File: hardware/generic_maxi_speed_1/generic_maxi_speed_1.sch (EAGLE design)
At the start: 30 parts, among them IC1 MEGA168/328, IC2 RFM12, IC3 LP2950Z, Q1 20MHz

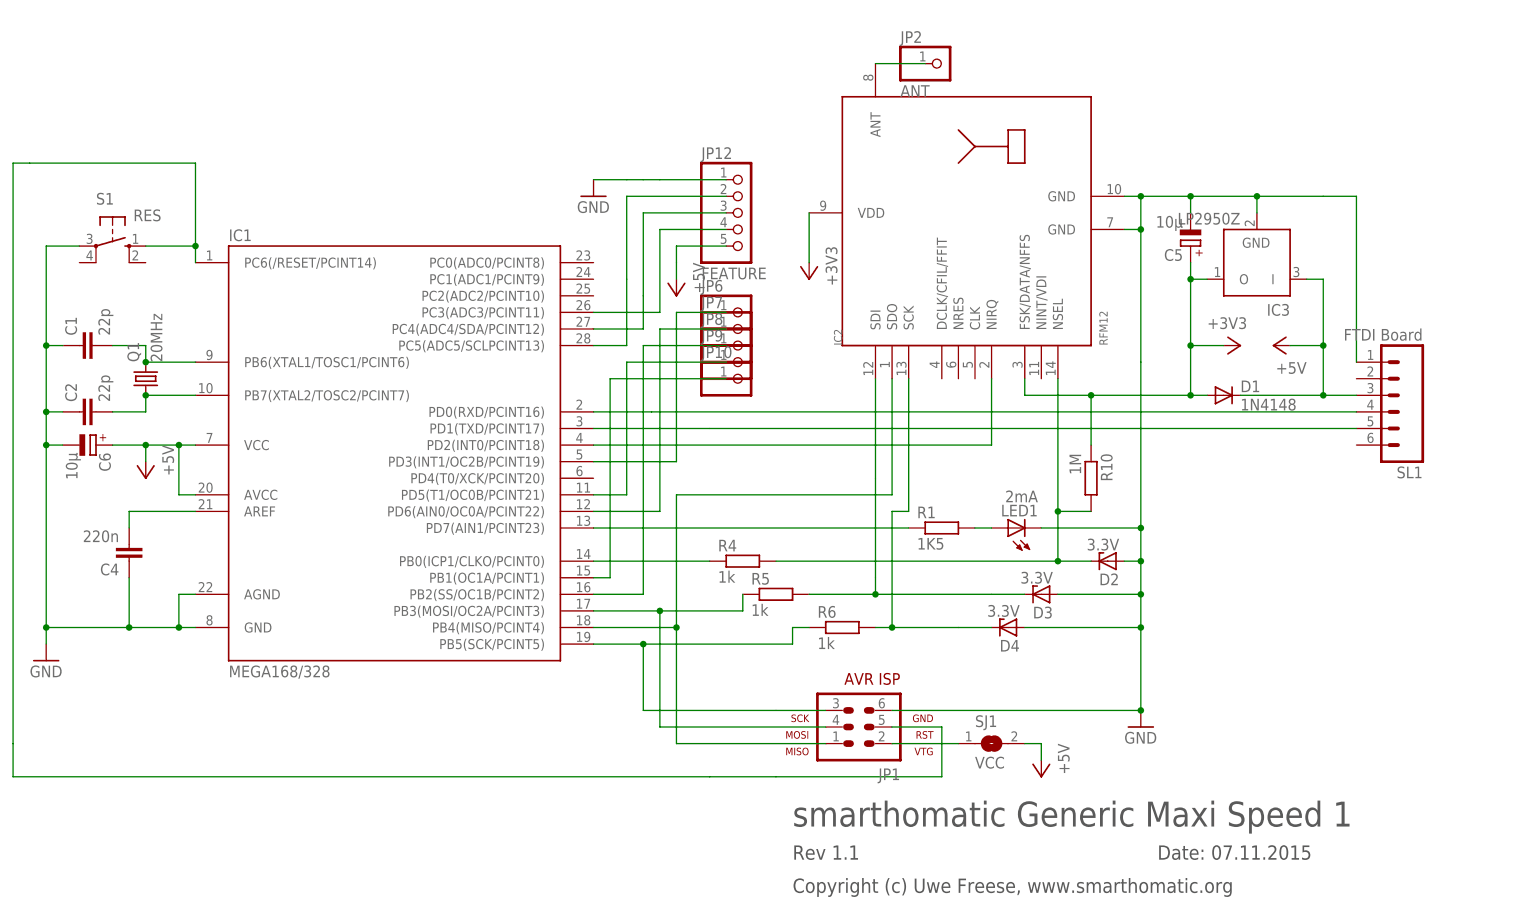
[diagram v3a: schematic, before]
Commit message: Generic Maxi Speed V1.2: Added transistor to switch power of RFM module to allow restart or module if transceiver doesn't react anymore.
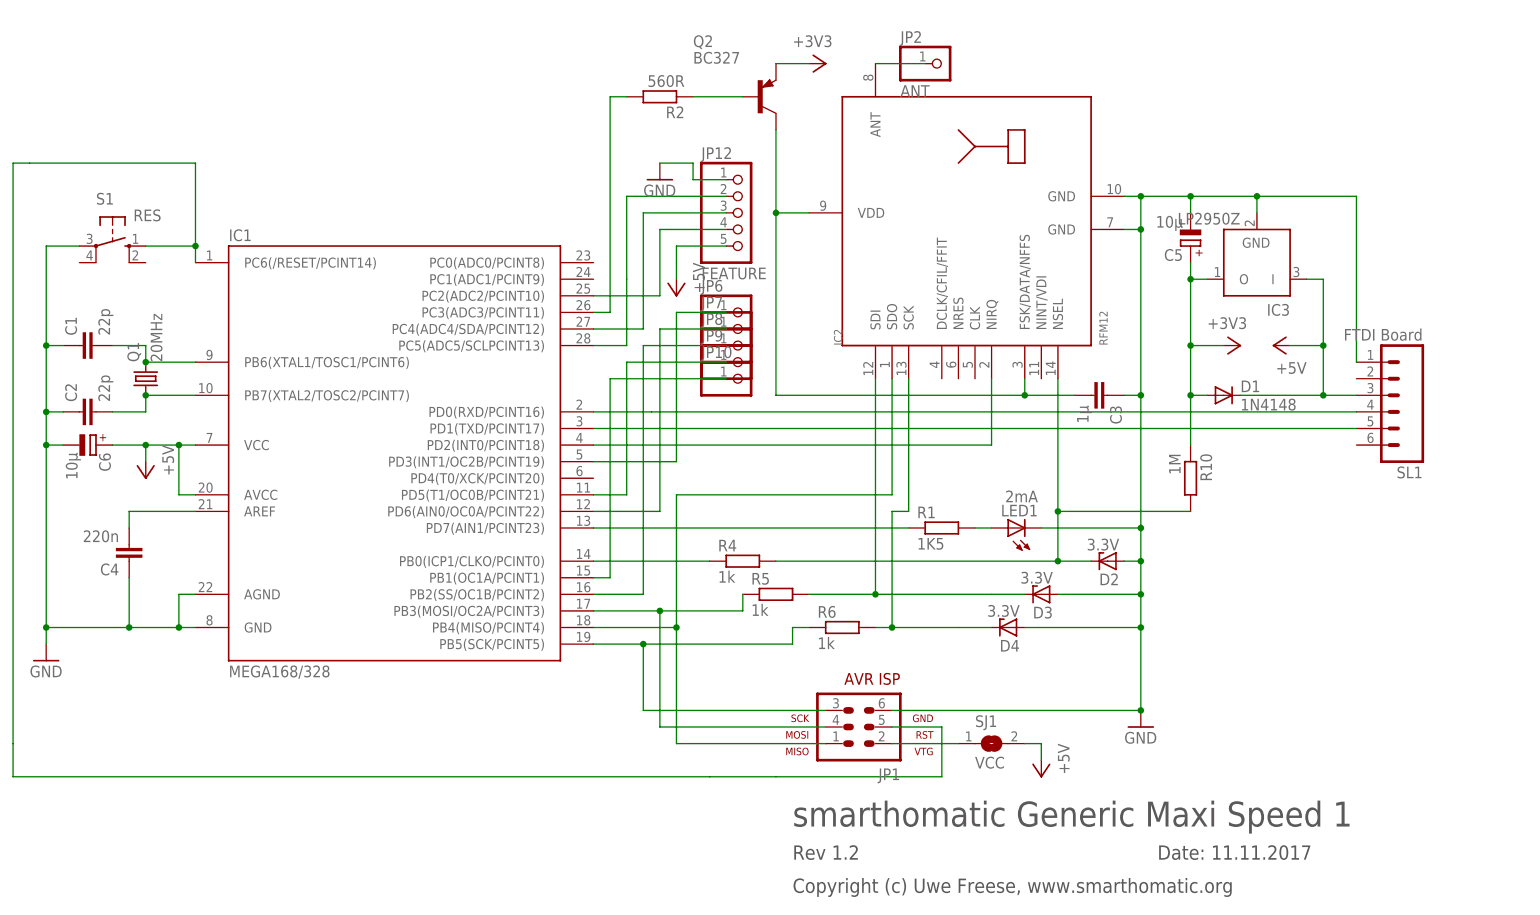
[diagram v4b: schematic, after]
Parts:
- added C3: 1µ, rcl:C-EU025-030X050
- added Q2: BC327, transistor-pnp:BC327
- added R2: 560R, rcl:R-EU_0207/7
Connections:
- new net N$28: IC1.PC3(ADC3/PCINT11), R2.2
- new net N$29: Q2.B, R2.1
- new net N$32: C3.2, IC2.FSK/DATA/NFFS, IC2.VDD, Q2.C
- net +3V3: now also Q2.E; no longer IC2.FSK/DATA/NFFS, IC2.VDD
- net GND: now also C3.1
- net N$14: now also IC1.PC2(ADC2/PCINT10); no longer IC1.PC3(ADC3/PCINT11)
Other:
- note added: "Date: 11.11.2017"
- note added: "Rev 1.2"
- note removed: "Date: 07.11.2015"
- note removed: "Rev 1.1"
- moved on the sheet: R10
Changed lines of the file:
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@@
 <?xml version="1.0" encoding="utf-8"?>
 <!DOCTYPE eagle SYSTEM "eagle.dtd">
-<eagle version="7.3.0">
+<eagle version="7.1.0">
 <drawing>
 <settings>
@@
 <part name="SJ1" library="jumper" deviceset="SJ" device="" value="VCC"/>
 <part name="P+3" library="supply1" deviceset="+5V" device=""/>
+<part name="Q2" library="transistor-pnp" deviceset="BC327" device=""/>
+<part name="R2" library="rcl" deviceset="R-EU_" device="0207/7" value="560R"/>
+<part name="C3" library="rcl" deviceset="C-EU" device="025-030X050" value="1µ"/>
 </parts>
 <sheets>
@@
 <frame x1="-60.96" y1="-58.42" x2="172.72" y2="93.98" columns="8" rows="5" layer="97"/>
 <text x="66.04" y="-40.64" size="3.81" layer="97">smarthomatic Generic Maxi Speed 1</text>
-<text x="121.92" y="-45.72" size="2.1844" layer="97">Date: 07.11.2015</text>
-<text x="66.04" y="-45.72" size="2.1844" layer="97">Rev 1.1</text>
+<text x="121.92" y="-45.72" size="2.1844" layer="97">Date: 11.11.2017</text>
+<text x="66.04" y="-45.72" size="2.1844" layer="97">Rev 1.2</text>
 <text x="66.04" y="-50.8" size="2.1844" layer="97">Copyright (c) Uwe Freese, www.smarthomatic.org</text>
 </plain>
@@
 <attribute name="NAME" x="162.56" y="14.478" size="1.778" layer="95" rot="R180"/>
 </instance>
-<instance part="GND3" gate="1" x="35.56" y="55.88"/>
-<instance part="R10" gate="G$1" x="111.76" y="12.7" rot="R270"/>
+<instance part="GND3" gate="1" x="45.72" y="58.42"/>
+<instance part="R10" gate="G$1" x="127" y="12.7" rot="R270"/>
 <instance part="C1" gate="G$1" x="-43.18" y="33.02" rot="R90"/>
 <instance part="C2" gate="G$1" x="-43.18" y="22.86" rot="R90"/>
@@
 <instance part="IC3" gate="G$1" x="137.16" y="45.72" rot="R180"/>
 <instance part="D1" gate="G$1" x="132.08" y="25.4"/>
-<instance part="+3V1" gate="G$1" x="68.58" y="43.18" rot="R180"/>
+<instance part="+3V1" gate="G$1" x="71.12" y="76.2" rot="R270"/>
 <instance part="P+4" gate="1" x="-33.02" y="12.7" rot="R180"/>
 <instance part="P+1" gate="1" x="139.7" y="33.02" rot="R90"/>
@@
 <instance part="SJ1" gate="1" x="96.52" y="-27.94"/>
 <instance part="P+3" gate="1" x="104.14" y="-33.02" rot="R180"/>
+<instance part="Q2" gate="G$1" x="60.96" y="71.12"/>
+<instance part="R2" gate="G$1" x="45.72" y="71.12" rot="R180"/>
+<instance part="C3" gate="G$1" x="114.3" y="25.4" rot="R270"/>
 </instances>
 <busses>
@@
 <wire x1="81.28" y1="-22.86" x2="119.38" y2="-22.86" width="0.1524" layer="91"/>
 <pinref part="GND2" gate="1" pin="GND"/>
-<wire x1="119.38" y1="30.48" x2="119.38" y2="5.08" width="0.1524" layer="91"/>
 <junction x="119.38" y="-22.86"/>
 <pinref part="LED1" gate="G$1" pin="C"/>
+<wire x1="119.38" y1="25.4" x2="119.38" y2="5.08" width="0.1524" layer="91"/>
 <wire x1="119.38" y1="5.08" x2="119.38" y2="0" width="0.1524" layer="91"/>
 <wire x1="119.38" y1="0" x2="119.38" y2="-5.08" width="0.1524" layer="91"/>
@@
 <wire x1="104.14" y1="5.08" x2="119.38" y2="5.08" width="0.1524" layer="91"/>
 <junction x="119.38" y="5.08"/>
-<wire x1="119.38" y1="30.48" x2="119.38" y2="50.8" width="0.1524" layer="91"/>
+<wire x1="119.38" y1="25.4" x2="119.38" y2="50.8" width="0.1524" layer="91"/>
 <pinref part="IC2" gate="G$1" pin="GND@1"/>
 <wire x1="119.38" y1="50.8" x2="116.84" y2="50.8" width="0.1524" layer="91"/>
@@
 <pinref part="SL1" gate="G$1" pin="1"/>
 <wire x1="152.4" y1="30.48" x2="152.4" y2="55.88" width="0.1524" layer="91"/>
-<wire x1="137.16" y1="55.88" x2="147.32" y2="55.88" width="0.1524" layer="91"/>
+<wire x1="137.16" y1="55.88" x2="152.4" y2="55.88" width="0.1524" layer="91"/>
 <junction x="137.16" y="55.88"/>
-<wire x1="147.32" y1="55.88" x2="152.4" y2="55.88" width="0.1524" layer="91"/>
 <wire x1="106.68" y1="-5.08" x2="119.38" y2="-5.08" width="0.1524" layer="91"/>
 <junction x="119.38" y="-5.08"/>
@@
 <pinref part="D3" gate="G$1" pin="A"/>
 <pinref part="D4" gate="G$1" pin="A"/>
+<pinref part="C3" gate="G$1" pin="1"/>
+<wire x1="116.84" y1="25.4" x2="119.38" y2="25.4" width="0.1524" layer="91"/>
+<junction x="119.38" y="25.4"/>
 </segment>
 <segment>
 <pinref part="GND3" gate="1" pin="GND"/>
-<wire x1="40.64" y1="58.42" x2="35.56" y2="58.42" width="0.1524" layer="91"/>
-<wire x1="40.64" y1="58.42" x2="43.18" y2="58.42" width="0.1524" layer="91"/>
-<wire x1="43.18" y1="58.42" x2="45.72" y2="58.42" width="0.1524" layer="91"/>
+<wire x1="50.8" y1="58.42" x2="50.8" y2="60.96" width="0.1524" layer="91"/>
+<wire x1="50.8" y1="60.96" x2="45.72" y2="60.96" width="0.1524" layer="91"/>
 <pinref part="JP12" gate="A" pin="1"/>
-<wire x1="45.72" y1="58.42" x2="55.88" y2="58.42" width="0.1524" layer="91"/>
+<wire x1="50.8" y1="58.42" x2="55.88" y2="58.42" width="0.1524" layer="91"/>
 </segment>
 </net>
@@
 <net name="+3V3" class="0">
 <segment>
-<pinref part="+3V1" gate="G$1" pin="+3V3"/>
-<pinref part="IC2" gate="G$1" pin="VDD"/>
-<wire x1="68.58" y1="45.72" x2="68.58" y2="53.34" width="0.1524" layer="91"/>
-</segment>
-<segment>
-<wire x1="111.76" y1="25.4" x2="111.76" y2="17.78" width="0.1524" layer="91"/>
-<pinref part="IC2" gate="G$1" pin="FSK/DATA/NFFS"/>
-<wire x1="101.6" y1="27.94" x2="101.6" y2="25.4" width="0.1524" layer="91"/>
-<wire x1="101.6" y1="25.4" x2="111.76" y2="25.4" width="0.1524" layer="91"/>
+<wire x1="127" y1="25.4" x2="127" y2="17.78" width="0.1524" layer="91"/>
 <pinref part="R10" gate="G$1" pin="1"/>
 <pinref part="IC3" gate="G$1" pin="O"/>
@@
 <wire x1="127" y1="43.18" x2="127" y2="33.02" width="0.1524" layer="91"/>
 <wire x1="127" y1="33.02" x2="127" y2="25.4" width="0.1524" layer="91"/>
-<wire x1="127" y1="25.4" x2="111.76" y2="25.4" width="0.1524" layer="91"/>
-<junction x="111.76" y="25.4"/>
 <pinref part="D1" gate="G$1" pin="A"/>
 <wire x1="127" y1="25.4" x2="129.54" y2="25.4" width="0.1524" layer="91"/>
@@
 <wire x1="127" y1="43.18" x2="127" y2="45.72" width="0.1524" layer="91"/>
 <junction x="127" y="43.18"/>
+</segment>
+<segment>
+<pinref part="Q2" gate="G$1" pin="E"/>
+<wire x1="68.58" y1="76.2" x2="63.5" y2="76.2" width="0.1524" layer="91"/>
+<pinref part="+3V1" gate="G$1" pin="+3V3"/>
 </segment>
 </net>
@@
 <net name="N$14" class="0">
 <segment>
-<wire x1="45.72" y1="38.1" x2="45.72" y2="50.8" width="0.1524" layer="91"/>
 <wire x1="45.72" y1="50.8" x2="55.88" y2="50.8" width="0.1524" layer="91"/>
-<pinref part="IC1" gate="1" pin="PC3(ADC3/PCINT11)"/>
-<wire x1="45.72" y1="38.1" x2="35.56" y2="38.1" width="0.1524" layer="91"/>
 <pinref part="JP12" gate="A" pin="4"/>
+<pinref part="IC1" gate="1" pin="PC2(ADC2/PCINT10)"/>
+<wire x1="35.56" y1="40.64" x2="45.72" y2="40.64" width="0.1524" layer="91"/>
+<wire x1="45.72" y1="40.64" x2="45.72" y2="50.8" width="0.1524" layer="91"/>
 </segment>
 </net>
@@
 <wire x1="63.5" y1="0" x2="106.68" y2="0" width="0.1524" layer="91"/>
 <pinref part="IC2" gate="G$1" pin="NSEL"/>
-<wire x1="111.76" y1="7.62" x2="106.68" y2="7.62" width="0.1524" layer="91"/>
+<wire x1="127" y1="7.62" x2="106.68" y2="7.62" width="0.1524" layer="91"/>
 <pinref part="R10" gate="G$1" pin="2"/>
 <wire x1="106.68" y1="7.62" x2="106.68" y2="27.94" width="0.1524" layer="91"/>
@@
 </segment>
 </net>
+<net name="N$28" class="0">
+<segment>
+<pinref part="IC1" gate="1" pin="PC3(ADC3/PCINT11)"/>
+<wire x1="35.56" y1="38.1" x2="38.1" y2="38.1" width="0.1524" layer="91"/>
+<wire x1="38.1" y1="38.1" x2="38.1" y2="71.12" width="0.1524" layer="91"/>
+<pinref part="R2" gate="G$1" pin="2"/>
+<wire x1="38.1" y1="71.12" x2="40.64" y2="71.12" width="0.1524" layer="91"/>
+</segment>
+</net>
+<net name="N$29" class="0">
+<segment>
+<pinref part="R2" gate="G$1" pin="1"/>
+<pinref part="Q2" gate="G$1" pin="B"/>
+<wire x1="50.8" y1="71.12" x2="58.42" y2="71.12" width="0.1524" layer="91"/>
+</segment>
+</net>
+<net name="N$32" class="0">
+<segment>
+<pinref part="IC2" gate="G$1" pin="FSK/DATA/NFFS"/>
+<wire x1="101.6" y1="27.94" x2="101.6" y2="25.4" width="0.1524" layer="91"/>
+<pinref part="Q2" gate="G$1" pin="C"/>
+<wire x1="63.5" y1="66.04" x2="63.5" y2="53.34" width="0.1524" layer="91"/>
+<pinref part="IC2" gate="G$1" pin="VDD"/>
+<wire x1="63.5" y1="53.34" x2="68.58" y2="53.34" width="0.1524" layer="91"/>
+<wire x1="101.6" y1="25.4" x2="63.5" y2="25.4" width="0.1524" layer="91"/>
+<wire x1="63.5" y1="25.4" x2="63.5" y2="53.34" width="0.1524" layer="91"/>
+<junction x="63.5" y="53.34"/>
+<pinref part="C3" gate="G$1" pin="2"/>
+<wire x1="101.6" y1="25.4" x2="109.22" y2="25.4" width="0.1524" layer="91"/>
+<junction x="101.6" y="25.4"/>
+</segment>
+</net>
